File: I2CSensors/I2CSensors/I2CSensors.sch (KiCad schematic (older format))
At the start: 16 parts, among them J1 Conn_01x04_Male, U1 BME280, U2 LSM9DS1

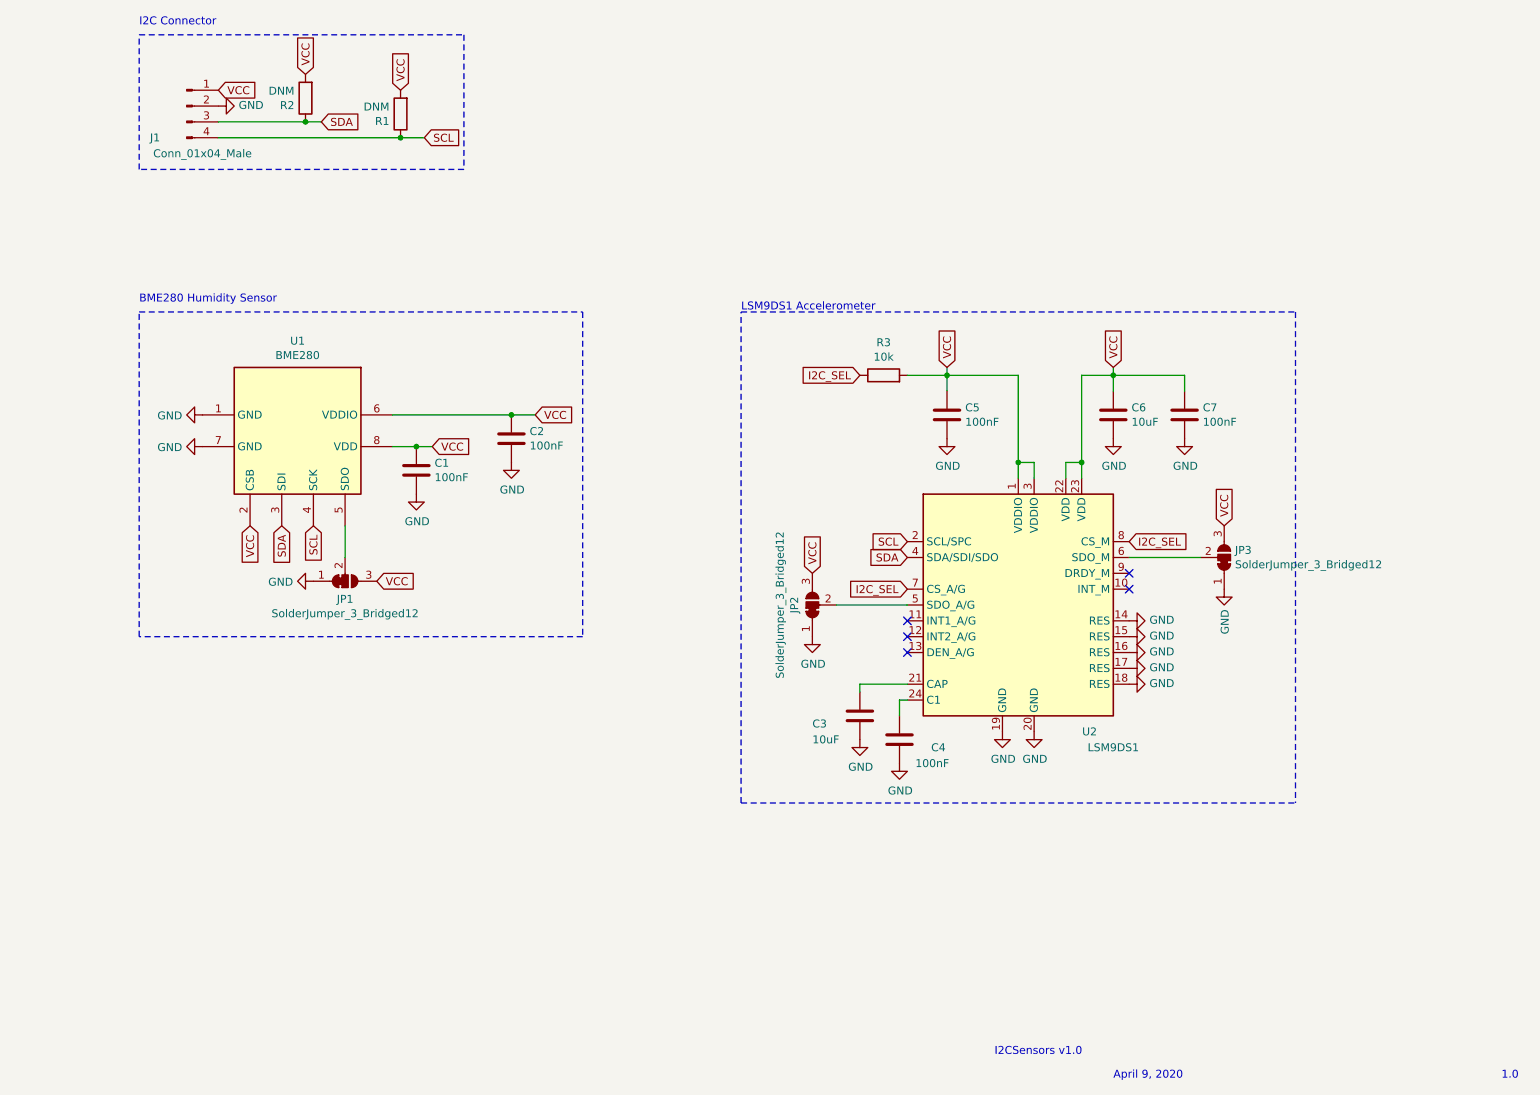
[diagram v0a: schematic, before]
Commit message: Added i2c accel to msp430.
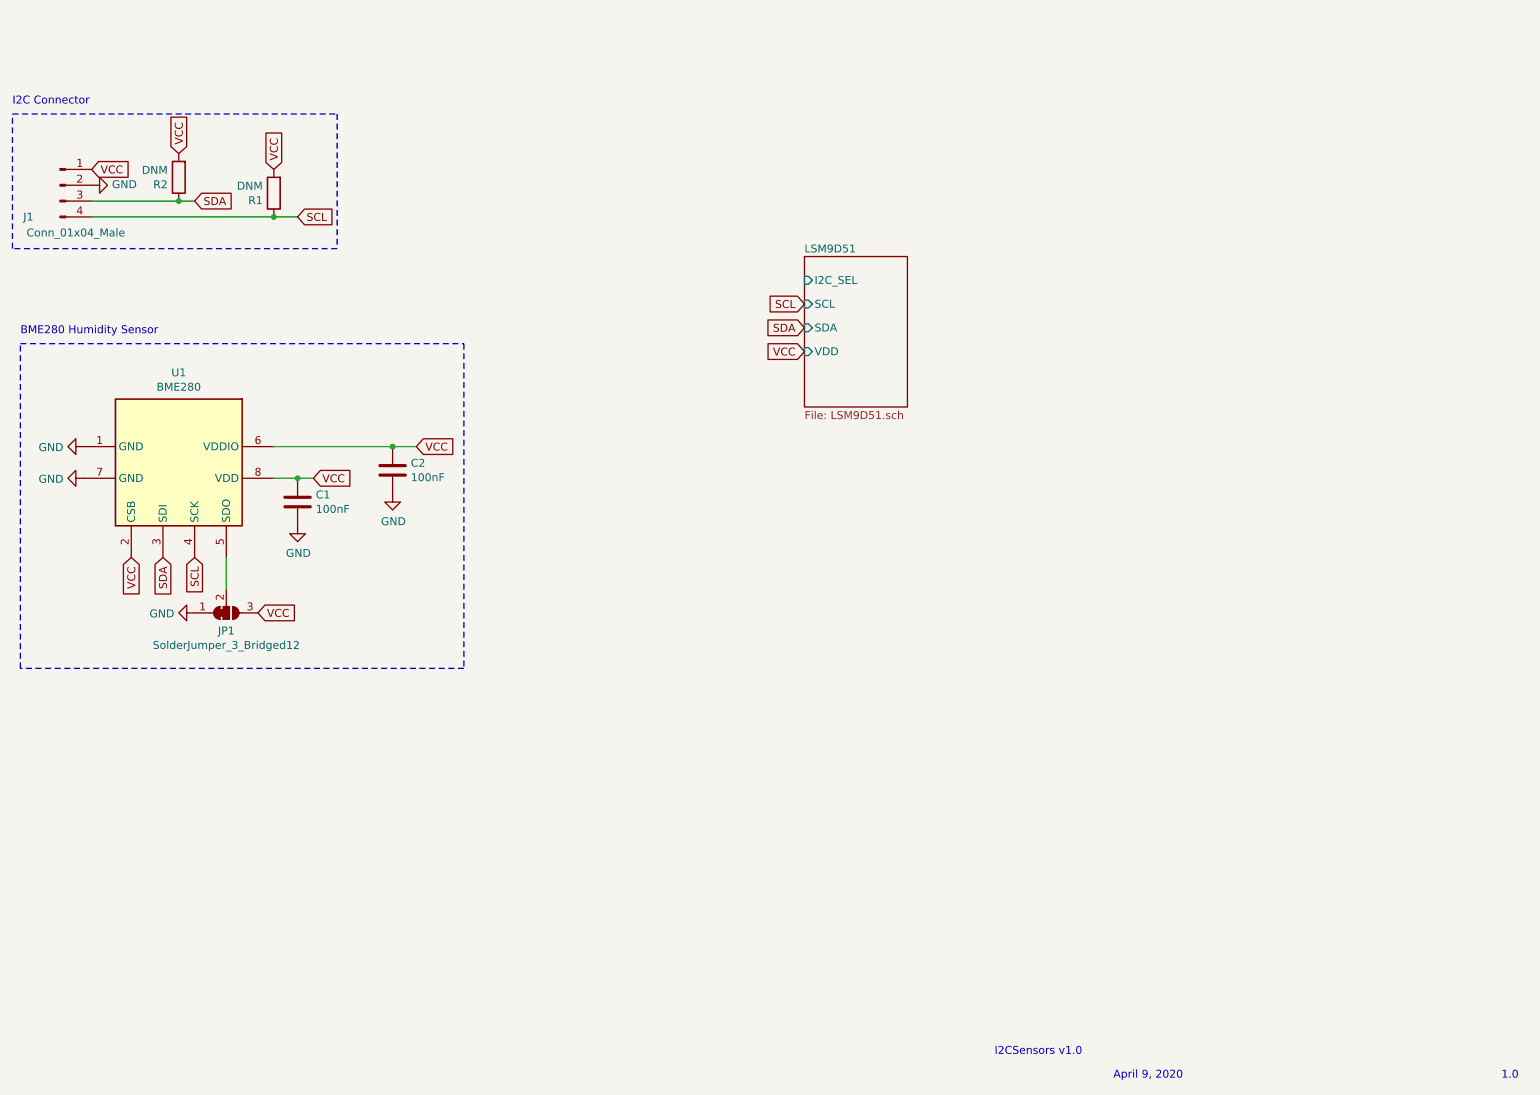
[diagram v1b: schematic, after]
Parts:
- removed C3, C6: 10uF, Capacitor_SMD:C_0603_1608Metric_Pad1.05x0.95mm_HandSolder, symbol Device:C
- removed C4, C5, C7: 100nF, Capacitor_SMD:C_0603_1608Metric_Pad1.05x0.95mm_HandSolder, symbol Device:C
- removed JP2, JP3: SolderJumper_3_Bridged12, Jumper:SolderJumper-3_P1.3mm_Bridged12_RoundedPad1.0x1.5mm, symbol Jumper:SolderJumper_3_Bridged12
- removed R3: 10k, Resistor_SMD:R_0603_1608Metric_Pad1.05x0.95mm_HandSolder, symbol Device:R
- removed U2: LSM9DS1, Package_LGA:LGA-24L_3x3.5mm_P0.43mm, symbol Sensor_Motion:LSM9DS1
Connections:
- no-connect marks 5 -> 0
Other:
- note removed: "LSM9DS1 Accelerometer"
- moved on the sheet: C1, C2, J1, JP1, R1, R2, U1
